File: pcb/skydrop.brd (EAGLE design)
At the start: 103 x 83 mm, 99 parts, among them IC1 RT9193-33GB, IC2 MCP73831/OT, IC3 STM809SWX6F, IC4 MS5611-01BA03, Q1 BSS84, Q10 BSS84, Q2 BSS123, Q3 BSS123, Q4 BSS84, Q5 BSS84, Q6 BSS84, Q7 BSS123, Q8 BSS84, Q9 BSS84, U2 W25Q16BVSS

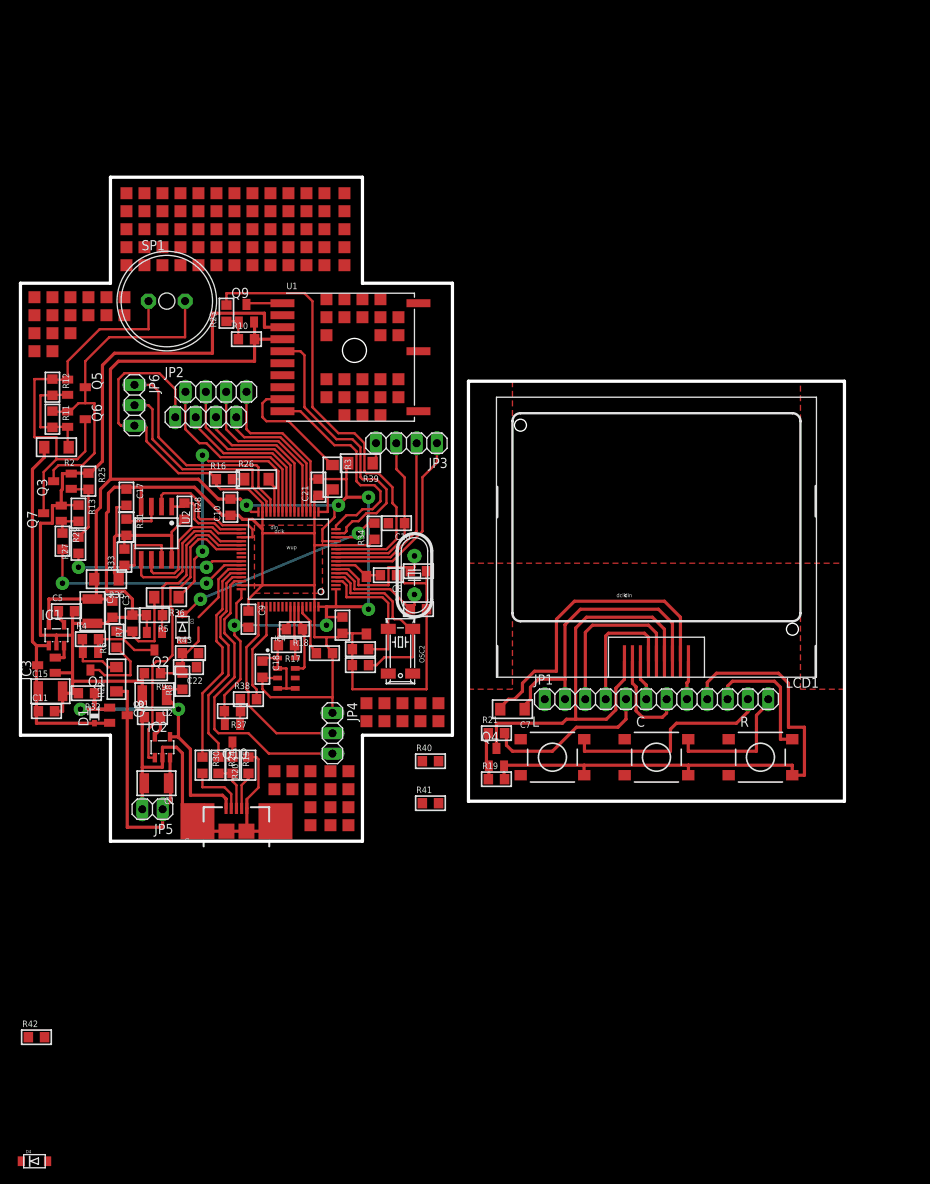
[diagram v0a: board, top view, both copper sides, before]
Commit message: start spi flash support
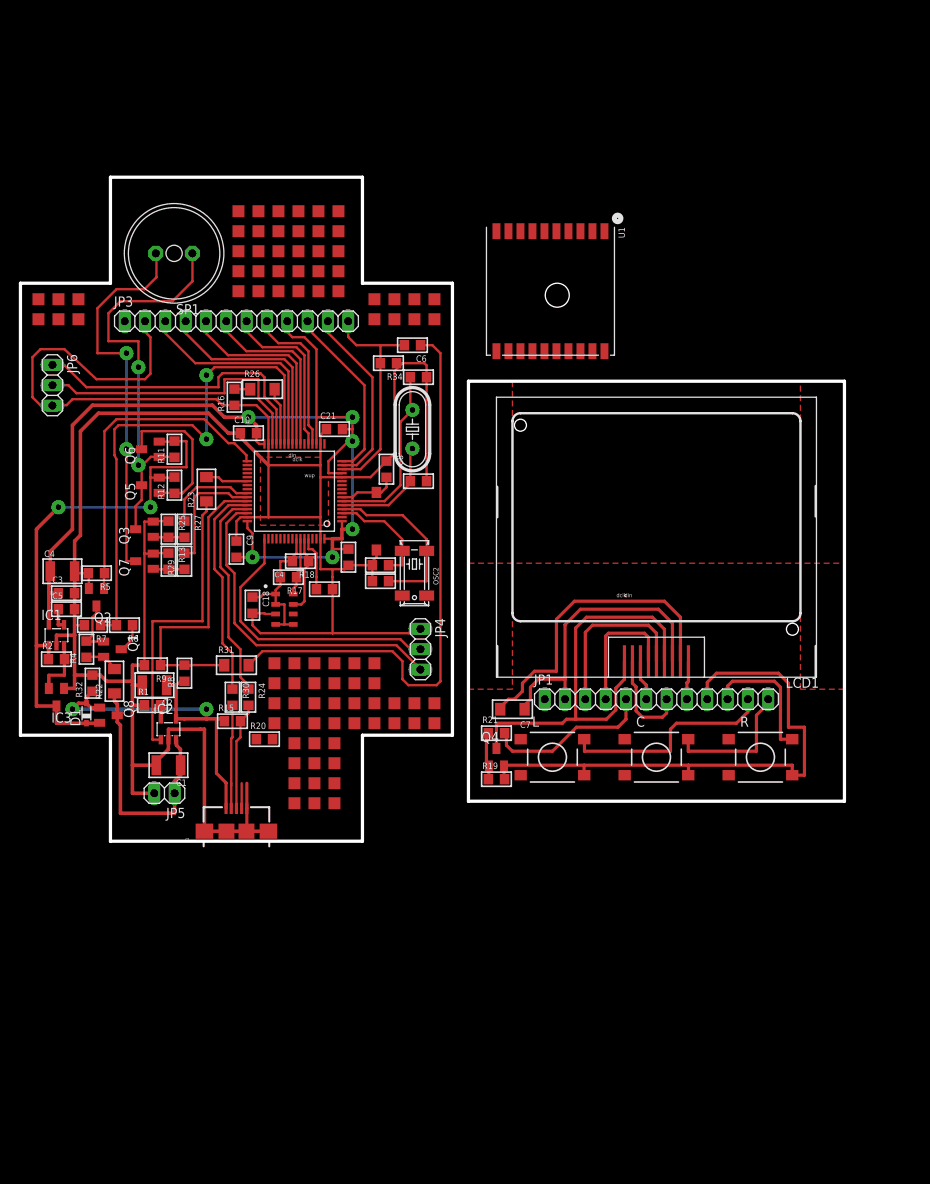
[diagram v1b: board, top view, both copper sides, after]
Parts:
- removed C11, C17: (no value), skydrop:C0805
- removed C15: (no value), skydrop:C1210
- removed C16, C22: 0.01uf, skydrop:C0805
- removed D3, D4: (no value), skydrop:SOD-123FL
- removed JP2: (no value), skydrop:1X08
- removed Q10, Q9: BSS84, transistor-small-signal:SOT23
- removed R10, R28, R33, R37: 10k, skydrop:R0805
- removed R3, R35, R36, R39: 0, skydrop:R1206
- removed R38: 100, skydrop:R0805
- removed R40, R41, R42, R43: 47k, skydrop:R0805
- removed U2: W25Q16BVSS, skydrop:SO08-SS
- added C6: (no value), skydrop:C0805
- JP3: device pinhead:1X04 -> pinhead:1X12
- R2: device skydrop:R1206 -> skydrop:R0805
- R23: value 100 -> 0; device skydrop:R0805 -> skydrop:R1206
- R31: value 10k -> 0; device skydrop:R0805 -> skydrop:R1206
- R8: value 3.3k -> (none)
- R9: value 10k -> (none)
- U1: device skydrop:FGPMMOPA6C -> adafruit:FGPMMOPA6H
- moved R2 26.5 mm to (7.00, 23.2), turned to 0 degrees
- moved U1 26.3 mm to (68.8, 69.2), turned to 270 degrees
- moved JP3 26.2 mm to (29.5, 65.5), turned to 0 degrees
- moved C13 24.2 mm to (52.2, 58.5)
- moved R23 22.1 mm to (25.8, 44.5)
- moved R31 22.1 mm to (29.5, 22.5), turned to 0 degrees
- moved R34 21.1 mm to (48.5, 60.2), turned to 180 degrees
- moved R12 19.6 mm to (21.8, 45.0), turned to 90 degrees
- moved OSC 18.3 mm to (51.5, 52.0)
- moved C12 16.0 mm to (52.2, 45.5)
- moved R11 15.7 mm to (21.8, 49.5), turned to 90 degrees
- moved R29 15.5 mm to (23.0, 35.5), turned to 90 degrees
- moved Q5 15.4 mm to (18.8, 45.0), turned to 90 degrees
- moved JP4 15.2 mm to (52.5, 24.5)
- moved R27 13.4 mm to (23.0, 39.5), turned to 270 degrees
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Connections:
- removed net BTN_C_B1: C22.1, R42.1
- removed net FLASH_CLK: U2.6, UC1.P$34
- removed net FLASH_CS: R28.1, U2.1, UC1.P$33
- removed net FLASH_DI: U2.5, UC1.P$36
- removed net FLASH_DO: U2.2, UC1.P$35
- removed net GPS_3D_FIX: U1.P$5, UC1.P$15
- removed net GPS_PWR: R23.2, UC1.P$11
- removed net GPS_RX: U1.P$10, UC1.P$16
- removed net GPS_TX: R3.2, UC1.P$17
- removed net N$1: Q5.2, Q6.2, R11.2, R12.2, R2.1
- removed net N$17: R3.1, U1.P$9
- removed net N$18: Q9.1, R10.1, R23.1
- removed net N$28: R31.1, U2.3
- removed net N$37: C17.2, R28.2, R31.2, R33.2, R35.1, U2.8
- removed net N$38: R36.2, R6.2, R7.1
- removed net N$39: Q10.1, R37.1, R38.1
- removed net N$43: Q10.3, R15.1
- removed net N$44: JP3.4, R39.1
- removed net N$45: C16.2, D4.A, R41.1
- removed net N$46: C22.2, D3.A, R43.1
- removed net USB_CON: R38.2, UC1.P$51
- removed net USB_VBUS: R8.2, R9.1, UC1.P$43
- removed net WAKE_UP: D3.C, D4.C, R34.2, UC1.P$14
- new net SND_1N: UC1.P$34
- new net SND_2N: UC1.P$35
- new net USB_U: R31.1, R8.2, R9.1, UC1.P$43
- net +5V: now also R15.1
- net BAT_EN: now also UC1.P$33; no longer UC1.P$37
- net BAT_SNS: now also R6.2, R7.1; no longer R36.1
- net BTN_C_B: now also C6.2, JP3.12, R34.2, UC1.P$14; no longer C16.1, JP3.3, R40.1, UC1.P$10
- net BTN_L_B: now also JP3.11, UC1.P$15; no longer JP3.2, UC1.P$9
- net BTN_R_B: now also JP3.10, UC1.P$16; no longer JP3.1, UC1.P$8
- net CHARGE_STAT: now also R23.2; no longer IC2.1
- net GND: now also JP3.2; no longer C11.2, C15.2, C17.1, JP2.1, R40.2, R41.2, R42.2, R43.2, U1.P$3, U2.4
- net LCD_CE_B: now also JP3.3; no longer JP2.2
- net LCD_CLK_B: now also JP3.7; no longer JP2.6
- net LCD_DC_B: now also JP3.4; no longer JP2.3
- net LCD_DIN_B: now also JP3.6; no longer JP2.5
- net LCD_PWR_B: now also JP3.5; no longer JP2.4
- net LCD_RST_B: now also JP3.8; no longer JP2.7
- net N$23: now also IC2.1, R23.1; no longer R33.1, U2.7
- net N$30: now also C6.1, R31.2; no longer Q9.3, U1.P$1
- net N$5: now also R2.2
- net SND_PWR: now also Q5.2, Q6.2, R11.2, R12.2, R2.1; no longer C11.1, C15.1, R2.2
- net VCC: now also JP3.9; no longer JP2.8, Q10.2, Q9.2, R10.2, R35.2, R37.2, R39.2, U1.P$4
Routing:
- net N$30: track 4.65 -> 71.9 mm
- net VCC: track 200.0 -> 140.1 mm
- net GPS_PWR: track 56.9 -> 0.00 mm
- net USB_U: track 0.00 -> 39.7 mm
- net GPS_3D_FIX: track 36.1 -> 0.00 mm
- net CHARGE_STAT: track 38.2 -> 5.33 mm
- net BAT_SNS: track 34.4 -> 66.1 mm
- net WAKE_UP: track 30.2 -> 0.00 mm, vias 2 -> 0
- net N$23: track 8.98 -> 37.3 mm
- net GPS_RX: track 27.1 -> 0.00 mm
- net N$37: track 25.2 -> 0.00 mm
- net SND_PWR: track 46.4 -> 70.3 mm, vias 0 -> 2
- net BAT_EN: track 20.9 -> 40.8 mm
- net FLASH_DI: track 19.5 -> 0.00 mm
- net N$42: track 50.2 -> 69.7 mm, vias 0 -> 2
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
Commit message: pcb improovment, gitignore change
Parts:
- removed C6: (no value), skydrop:C0805
- added C11, C17: (no value), skydrop:C0805
- added C15: (no value), skydrop:C1210
- added C16, C22: 0.01uf, skydrop:C0805
- added D3, D4: (no value), skydrop:SOD-123FL
- added JP2: (no value), skydrop:1X08
- added Q10, Q9: BSS84, transistor-small-signal:SOT23
- added R10, R28, R33, R37: 10k, skydrop:R0805
- added R3, R35, R36, R39: 0, skydrop:R1206
- added R38: 100, skydrop:R0805
- added R40, R41, R42, R43: 47k, skydrop:R0805
- added U2: W25Q16BVSS, skydrop:SO08-SS
- JP3: device pinhead:1X12 -> pinhead:1X04
- R2: device skydrop:R0805 -> skydrop:R1206
- R23: value 0 -> 100; device skydrop:R1206 -> skydrop:R0805
- R31: value 0 -> 10k; device skydrop:R1206 -> skydrop:R0805
- R8: value (none) -> 3.3k
- R9: value (none) -> 10k
- U1: device adafruit:FGPMMOPA6H -> skydrop:FGPMMOPA6C
- moved R2 26.5 mm to (7.00, 49.8), turned to 180 degrees
- moved U1 26.3 mm to (43.8, 61.0), turned to 0 degrees
- moved JP3 26.2 mm to (50.8, 50.2), turned to 180 degrees
- moved C13 24.2 mm to (52.2, 34.2)
- moved R23 22.1 mm to (28.2, 66.5)
- moved R31 22.1 mm to (15.8, 39.8), turned to 270 degrees
- moved R34 21.1 mm to (46.8, 39.2), turned to 90 degrees
- moved R12 19.6 mm to (6.50, 57.2), turned to 270 degrees
- moved OSC 18.3 mm to (51.8, 33.8)
- moved C12 16.0 mm to (52.2, 29.5)
- moved R11 15.7 mm to (6.50, 53.2), turned to 270 degrees
- moved R29 15.5 mm to (7.75, 38.0), turned to 270 degrees
- moved Q5 15.4 mm to (9.50, 57.2), turned to 270 degrees
- moved JP4 15.2 mm to (41.5, 14.0)
- moved R27 13.4 mm to (9.75, 37.5), turned to 90 degrees
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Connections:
- removed net SND_1N: UC1.P$34
- removed net SND_2N: UC1.P$35
- removed net USB_U: R31.1, R8.2, R9.1, UC1.P$43
- new net BTN_C_B1: C22.1, R42.1
- new net FLASH_CLK: U2.6, UC1.P$34
- new net FLASH_CS: R28.1, U2.1, UC1.P$33
- new net FLASH_DI: U2.5, UC1.P$36
- new net FLASH_DO: U2.2, UC1.P$35
- new net GPS_3D_FIX: U1.P$5, UC1.P$15
- new net GPS_PWR: R23.2, UC1.P$11
- new net GPS_RX: U1.P$10, UC1.P$16
- new net GPS_TX: R3.2, UC1.P$17
- new net N$1: Q5.2, Q6.2, R11.2, R12.2, R2.1
- new net N$17: R3.1, U1.P$9
- new net N$18: Q9.1, R10.1, R23.1
- new net N$28: R31.1, U2.3
- new net N$37: C17.2, R28.2, R31.2, R33.2, R35.1, U2.8
- new net N$38: R36.2, R6.2, R7.1
- new net N$39: Q10.1, R37.1, R38.1
- new net N$43: Q10.3, R15.1
- new net N$44: JP3.4, R39.1
- new net N$45: C16.2, D4.A, R41.1
- new net N$46: C22.2, D3.A, R43.1
- new net USB_CON: R38.2, UC1.P$51
- new net USB_VBUS: R8.2, R9.1, UC1.P$43
- new net WAKE_UP: D3.C, D4.C, R34.2, UC1.P$14
- net +5V: no longer R15.1
- net BAT_EN: now also UC1.P$37; no longer UC1.P$33
- net BAT_SNS: now also R36.1; no longer R6.2, R7.1
- net BTN_C_B: now also C16.1, JP3.3, R40.1, UC1.P$10; no longer C6.2, JP3.12, R34.2, UC1.P$14
- net BTN_L_B: now also JP3.2, UC1.P$9; no longer JP3.11, UC1.P$15
- net BTN_R_B: now also JP3.1, UC1.P$8; no longer JP3.10, UC1.P$16
- net CHARGE_STAT: now also IC2.1; no longer R23.2
- net GND: now also C11.2, C15.2, C17.1, JP2.1, R40.2, R41.2, R42.2, R43.2, U1.P$3, U2.4; no longer JP3.2
- net LCD_CE_B: now also JP2.2; no longer JP3.3
- net LCD_CLK_B: now also JP2.6; no longer JP3.7
- net LCD_DC_B: now also JP2.3; no longer JP3.4
- net LCD_DIN_B: now also JP2.5; no longer JP3.6
- net LCD_PWR_B: now also JP2.4; no longer JP3.5
- net LCD_RST_B: now also JP2.7; no longer JP3.8
- net N$23: now also R33.1, U2.7; no longer IC2.1, R23.1
- net N$30: now also Q9.3, U1.P$1; no longer C6.1, R31.2
- net N$5: no longer R2.2
- net SND_PWR: now also C11.1, C15.1, R2.2; no longer Q5.2, Q6.2, R11.2, R12.2, R2.1
- net VCC: now also JP2.8, Q10.2, Q9.2, R10.2, R35.2, R37.2, R39.2, U1.P$4; no longer JP3.9
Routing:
- net N$30: track 71.9 -> 4.65 mm
- net VCC: track 140.1 -> 200.0 mm
- net GPS_PWR: track 0.00 -> 56.9 mm
- net USB_U: track 39.7 -> 0.00 mm
- net GPS_3D_FIX: track 0.00 -> 36.1 mm
- net CHARGE_STAT: track 5.33 -> 38.2 mm
- net BAT_SNS: track 66.1 -> 34.4 mm
- net WAKE_UP: track 0.00 -> 30.2 mm, vias 0 -> 2
- net N$23: track 37.3 -> 8.98 mm
- net GPS_RX: track 0.00 -> 27.1 mm
- net N$37: track 0.00 -> 25.2 mm
- net SND_PWR: track 70.3 -> 46.4 mm, vias 2 -> 0
- net BAT_EN: track 40.8 -> 20.9 mm
- net FLASH_DI: track 0.00 -> 19.5 mm
- net N$42: track 69.7 -> 50.2 mm, vias 2 -> 0
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
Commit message: improve pcb
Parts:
- removed R20: 100k, skydrop:R0805
- removed R42: 47k, skydrop:R0805
- added SD1: TF-HOLDER, skydrop:TF-PULL
- moved D4 90.2 mm to (50.0, 38.2)
- moved R40 35.9 mm to (51.0, 46.2)
- moved R41 35.6 mm to (51.0, 40.8)
- moved Q3 9.75 mm to (7.75, 55.2)
- moved Q5 9.75 mm to (9.50, 67.0)
- moved Q6 9.75 mm to (9.50, 63.0)
- moved Q7 9.75 mm to (6.50, 51.2)
- moved R11 9.75 mm to (6.50, 63.0)
- moved R12 9.75 mm to (6.50, 67.0)
- moved R13 9.75 mm to (9.75, 51.2)
- moved R2 9.75 mm to (7.00, 59.5)
- moved R25 9.75 mm to (11.0, 55.2)
- moved R27 9.75 mm to (9.75, 47.2)
- moved R29 9.75 mm to (7.75, 47.8)
- moved C18 7.29 mm to (39.0, 18.2), turned to 0 degrees
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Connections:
- removed net BTN_C_B1: C22.1, R42.1
- removed net N$40: J1.ID, R20.1
- new net VDD: SD1.4
- new net VSS: SD1.6
- net GND: no longer R20.2, R42.2
- net USB_VBUS: now also C22.1
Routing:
- net GND: track 376.7 -> 418.1 mm
- net SND_PWR: track 46.4 -> 56.2 mm
- net SND_2P: track 27.5 -> 37.3 mm
- net SND_1P: track 22.4 -> 32.2 mm
- net USB_VBUS: track 18.5 -> 27.4 mm
- net N$42: track 50.2 -> 42.4 mm
- net N$41: track 42.9 -> 35.7 mm
- net BTN_C_B: track 21.6 -> 28.3 mm
- net N$39: track 3.54 -> 9.73 mm
- net N$46: track 0.00 -> 5.66 mm
- net N$45: track 0.00 -> 5.41 mm
- net USB_CON: track 12.5 -> 7.55 mm
- net N$40: track 4.74 -> 0.00 mm
- net BTN_L_B: track 22.4 -> 27.0 mm
- net N$21: track 37.4 -> 33.8 mm
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
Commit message: [pcb] new display
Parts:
- removed C, L, R: DTSM-6, skydrop:DTSM-6
- removed C7: (no value), skydrop:C1206
- removed LCD1: LPH-7366, skydrop:LPH-7366
- removed Q4: BSS84, transistor-small-signal:SOT23
- removed R21: 100, skydrop:R0805
- removed SD1: TF-HOLDER, skydrop:TF-PULL
- added BTN_C, BTN_L, BTN_R: TS-1109-7, skydrop:SW4-6.2X6.2X5.0MM
- added C23, C24, C25, C6: 1uf, skydrop:C0805
- added C26: 3.3uf, skydrop:C0805
- added C27: 0.1uf, skydrop:C0805
- added C28: 10uf, skydrop:C0805
- added U$1: NOKIA5110, skydrop:NOKIA5110
- R19: value 10k -> 0; device skydrop:R0805 -> skydrop:R1206
- moved JP1 46.3 mm to (83.2, 64.5)
- moved R19 37.7 mm to (82.0, 40.2), turned to 270 degrees
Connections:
- removed net N$26: Q4.1, R19.1, R21.1
- removed net VDD: SD1.4
- removed net VSS: SD1.6
- new net N$15: C27.2, C28.2, R19.2, U$1.10, U$1.11, U$1.12, U$1.13, U$1.14, U$1.17, U$1.18, U$1.19, U$1.2, U$1.20, U$1.26, U$1.7, U$1.8, U$1.9
- new net N$40: C6.2, U$1.30
- new net N$47: C23.2, U$1.29
- new net N$48: C24.2, U$1.28
- new net N$49: C25.2, U$1.27
- new net N$50: C26.2, U$1.25
- new net N$52: BTN_R.2
- net BTN_C_T: now also BTN_C.3; no longer C.2
- net BTN_L_T: now also BTN_L.3; no longer L.2
- net BTN_R_T: now also BTN_R.3; no longer R.2
- net GND_T: now also C23.1, C24.1, C25.1, C26.1, C27.1, C28.1, C6.1, U$1.1, U$1.21, U$1.22, U$1.23, U$1.24, U$1.3; no longer C7.1, LCD1.7
- net LCD_CE_T: now also U$1.4; no longer LCD1.5
- net LCD_CLK_T: now also U$1.15; no longer LCD1.2
- net LCD_DC_T: now also U$1.6; no longer LCD1.4
- net LCD_DIN_T: now also U$1.16; no longer LCD1.3
- net LCD_PWR_T: no longer R21.2
- net LCD_RST_T: now also U$1.5; no longer LCD1.9
- net N$25: now also BTN_L.2; no longer LCD1.1, LCD1.6, Q4.3
- net N$36: now also BTN_C.2; no longer C7.2, LCD1.8
- net VCC_T: now also BTN_C.1, BTN_C.4, BTN_L.1, BTN_L.4, BTN_R.1, BTN_R.4, R19.1; no longer C.4, L.4, Q4.2, R.4, R19.2
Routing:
- net VCC_T: track 69.8 -> 155.5 mm
- net LCD_RST_T: track 4.83 -> 86.7 mm
- net LCD_DIN_T: track 5.05 -> 81.9 mm
- net BTN_R_T: track 16.8 -> 80.9 mm
- net LCD_CLK_T: track 12.5 -> 71.3 mm
- net LCD_DC_T: track 16.6 -> 71.5 mm
- net BTN_C_T: track 17.1 -> 71.3 mm
- net N$25: track 53.0 -> 0.00 mm
- net GND_T: track 36.8 -> 85.8 mm
- net LCD_CE_T: track 21.5 -> 67.0 mm
- net N$36: track 39.0 -> 0.00 mm
- net BTN_L_T: track 27.2 -> 64.8 mm
- net N$15: track 0.00 -> 37.3 mm
- net LCD_PWR_T: track 21.0 -> 0.00 mm
- net N$50: track 0.00 -> 17.9 mm
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- removed copper zone on layer 1, net N$15
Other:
- board size 103 x 83 mm -> 104.2 x 83 mm
